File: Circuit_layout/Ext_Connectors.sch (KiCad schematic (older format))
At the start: 9 parts, among them CON1 AVR-JTAG-10, J1 Spare_Conns, J4 Motor_Ctrl, J5 RJ12, P1 TSV, P2 CONN_02X10, P3 CONN_02X07

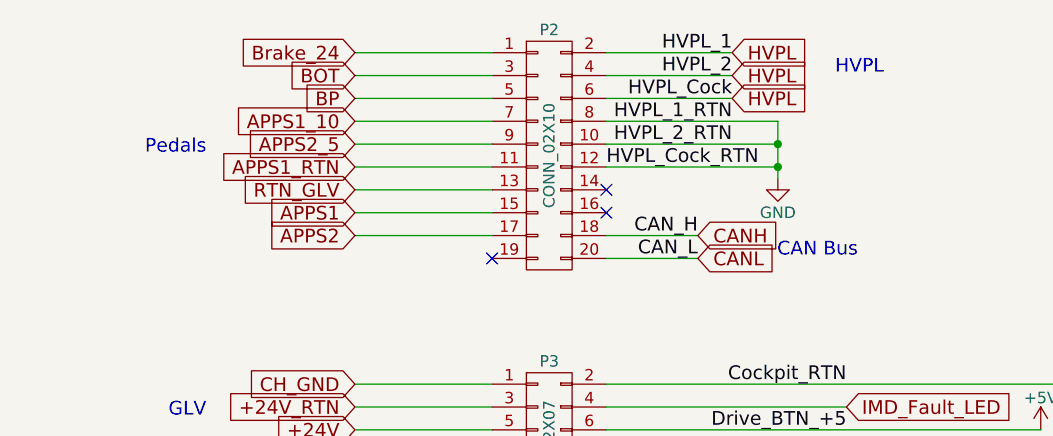
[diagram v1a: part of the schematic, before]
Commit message: organized sheet more, updated some footprints
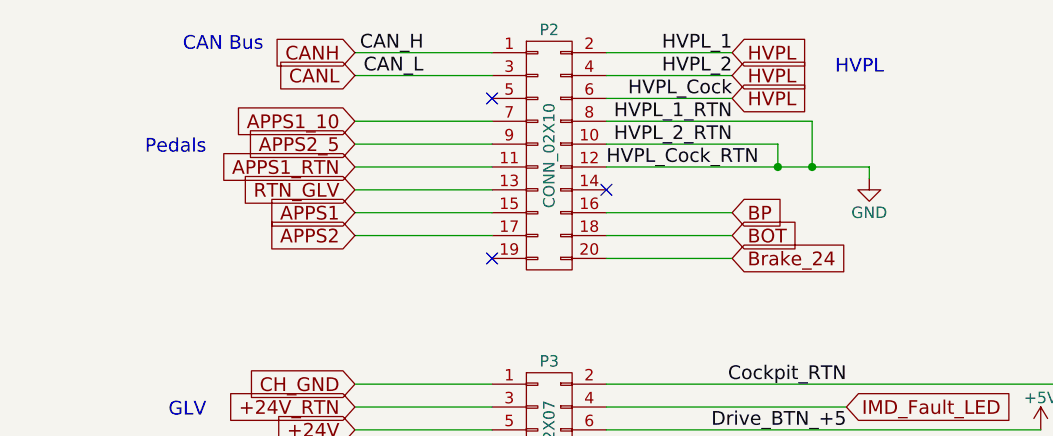
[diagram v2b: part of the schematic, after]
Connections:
- net BOT: now also P2.18 (P18); no longer P2.3 (P3)
- net BP: now also P2.16 (P16); no longer P2.5 (P5)
- net Brake_24: now also P2.20 (P20); no longer P2.1 (P1)
- net CANH: now also P2.1 (P1); no longer P2.18 (P18)
- net CANL: now also P2.3 (P3); no longer P2.20 (P20)
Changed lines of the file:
@@
 Text Label 7750 2700 2    60   ~ 0
 Drive_BTN_+5
-Text Label 7100 1950 2    60   ~ 0
+Text Label 5900 1150 2    60   ~ 0
 CAN_L
-Text Label 7100 1850 2    60   ~ 0
+Text Label 5900 1050 2    60   ~ 0
 CAN_H
 Text Label 7100 3100 2    60   ~ 0
@@
 Text Notes 4800 2900 0    60   ~ 0
 AIRs
-Text Notes 7800 1950 2    60   ~ 0
+Text Notes 5200 1050 2    60   ~ 0
 CAN Bus
 Text GLabel 1900 6450 2    60   Input ~ 0
@@
 Text GLabel 1900 6150 2    60   Input ~ 0
 +5HV
-Text GLabel 5600 1050 0    60   Input ~ 0
+Text GLabel 7250 1950 2    60   Input ~ 0
 Brake_24
-Text GLabel 5600 1150 0    60   Input ~ 0
+Text GLabel 7250 1850 2    60   Input ~ 0
 BOT
 Text GLabel 5600 1350 0    60   Input ~ 0
@@
 ~RESET_AVR
 $Comp
-L +5V #PWR022
+L +5V #PWR020
 U 1 1 58A81530
 P 6800 4400
-F 0 "#PWR022" H 6800 4250 50  0001 C CNN
+F 0 "#PWR020" H 6800 4250 50  0001 C CNN
 F 1 "+5V" H 6800 4540 50  0000 C CNN
 F 2 "" H 6800 4400 50  0000 C CNN
@@
 +24V_RTN
 $Comp
-L +24V #PWR023
+L +24V #PWR021
 U 1 1 58AF1C5B
 P 2250 1250
-F 0 "#PWR023" H 2250 1100 50  0001 C CNN
+F 0 "#PWR021" H 2250 1100 50  0001 C CNN
 F 1 "+24V" H 2250 1390 50  0000 C CNN
 F 2 "" H 2250 1250 50  0000 C CNN
@@
 Drive_LED
 $Comp
-L +5V #PWR024
+L +5V #PWR022
 U 1 1 58B1052B
 P 8600 2700
-F 0 "#PWR024" H 8600 2550 50  0001 C CNN
+F 0 "#PWR022" H 8600 2550 50  0001 C CNN
 F 1 "+5V" H 8600 2840 50  0000 C CNN
 F 2 "" H 8600 2700 50  0000 C CNN
@@
 Throttle_RTN
 $Comp
-L GND #PWR025
+L GND #PWR023
 U 1 1 58B4A72F
 P 7500 3150
-F 0 "#PWR025" H 7500 2900 50  0001 C CNN
+F 0 "#PWR023" H 7500 2900 50  0001 C CNN
 F 1 "GND" H 7500 3000 50  0000 C CNN
 F 2 "" H 7500 3150 50  0000 C CNN
@@
 CH_GND
 $Comp
-L GND #PWR026
+L GND #PWR024
 U 1 1 58B7A0E8
 P 8850 2700
-F 0 "#PWR026" H 8850 2450 50  0001 C CNN
+F 0 "#PWR024" H 8850 2450 50  0001 C CNN
 F 1 "GND" H 8850 2550 50  0000 C CNN
 F 2 "" H 8850 2700 50  0000 C CNN
@@
 CH_GND
 $Comp
-L GND #PWR027
+L GND #PWR025
 U 1 1 58B888D9
 P 2300 1900
-F 0 "#PWR027" H 2300 1650 50  0001 C CNN
+F 0 "#PWR025" H 2300 1650 50  0001 C CNN
 F 1 "GND" H 2300 1750 50  0000 C CNN
 F 2 "" H 2300 1900 50  0000 C CNN
@@
 +24V
 $Comp
-L PWR_FLAG #FLG028
+L PWR_FLAG #FLG026
 U 1 1 58B89230
 P 2550 1250
-F 0 "#FLG028" H 2550 1345 50  0001 C CNN
+F 0 "#FLG026" H 2550 1345 50  0001 C CNN
 F 1 "PWR_FLAG" H 2550 1430 50  0000 C CNN
 F 2 "" H 2550 1250 50  0000 C CNN
@@
 Text GLabel 7250 1250 2    60   Input ~ 0
 HVPL
-Text GLabel 7100 1850 2    60   Input ~ 0
+Text GLabel 5600 1050 0    60   Input ~ 0
 CANH
-Text GLabel 7100 1950 2    60   Input ~ 0
+Text GLabel 5600 1150 0    60   Input ~ 0
 CANL
 Text Notes 4950 2650 2    60   ~ 0
@@
 Spare_ADC_2
 $Comp
-L GND #PWR029
+L GND #PWR027
 U 1 1 58C3E939
-P 7450 1600
-F 0 "#PWR029" H 7450 1350 50  0001 C CNN
-F 1 "GND" H 7450 1450 50  0000 C CNN
-F 2 "" H 7450 1600 50  0000 C CNN
-F 3 "" H 7450 1600 50  0000 C CNN
-	1    7450 1600
+P 7850 1600
+F 0 "#PWR027" H 7850 1350 50  0001 C CNN
+F 1 "GND" H 7850 1450 50  0000 C CNN
+F 2 "" H 7850 1600 50  0000 C CNN
+F 3 "" H 7850 1600 50  0000 C CNN
+	1    7850 1600
 	-1   0    0    -1
 $EndComp
-Text GLabel 5600 1250 0    60   Input ~ 0
+Text GLabel 7250 1750 2    60   Input ~ 0
 BP
 Text Notes 7650 3100 0    60   ~ 0
 RTDS
 $Comp
-L GND #PWR030
+L GND #PWR028
 U 1 1 58D1CF0B
 P 6650 4900
-F 0 "#PWR030" H 6650 4650 50  0001 C CNN
+F 0 "#PWR028" H 6650 4650 50  0001 C CNN
 F 1 "GND" H 6650 4750 50  0000 C CNN
 F 2 "" H 6650 4900 50  0000 C CNN
@@
 I_RTN
 $Comp
-L PWR_FLAG #FLG031
+L PWR_FLAG #FLG029
 U 1 1 58D3F022
 P 2650 1900
-F 0 "#FLG031" H 2650 1995 50  0001 C CNN
+F 0 "#FLG029" H 2650 1995 50  0001 C CNN
 F 1 "PWR_FLAG" H 2650 2080 50  0000 C CNN
 F 2 "" H 2650 1900 50  0000 C CNN
@@
 $EndComp
 $Comp
-L +5V #PWR032
+L +5V #PWR030
 U 1 1 58D6E615
 P 3100 3950
-F 0 "#PWR032" H 3100 3800 50  0001 C CNN
+F 0 "#PWR030" H 3100 3800 50  0001 C CNN
 F 1 "+5V" H 3100 4090 50  0000 C CNN
 F 2 "" H 3100 3950 50  0000 C CNN
@@
 NoConn ~ 6200 1950
 NoConn ~ 6700 1650
-NoConn ~ 6700 1750
 Wire Wire Line
 	1150 6250 1900 6250
@@
 Wire Wire Line
 	6200 1350 5600 1350
-Wire Wire Line
-	6200 1050 5600 1050
 Wire Wire Line
 	1200 7150 1600 7150
@@
 	2250 7000 2250 7250
 Wire Wire Line
-	5600 1150 6200 1150
-Wire Wire Line
 	5600 3100 6200 3100
 Wire Wire Line
@@
 	8850 2500 6700 2500
 Wire Wire Line
-	6700 1950 7100 1950
-Wire Wire Line
-	7100 1850 6700 1850
-Wire Wire Line
 	5600 2600 6200 2600
 Wire Wire Line
@@
 	6700 1150 7250 1150
 Wire Wire Line
-	7450 1350 6700 1350
+	6700 1350 7600 1350
 Wire Wire Line
 	7450 1450 6700 1450
 Wire Wire Line
-	7450 1350 7450 1600
-Connection ~ 7450 1450
-Wire Wire Line
 	7500 3100 6700 3100
 Wire Wire Line
 	6700 3000 7100 3000
-Wire Wire Line
-	5600 1250 6200 1250
 Wire Wire Line
 	7500 3100 7500 3150
@@
 	3100 4050 3100 3950
 Wire Wire Line
-	6700 1550 7450 1550
+	6700 1550 7850 1550
+Wire Wire Line
+	7850 1550 7850 1600
+Wire Wire Line
+	7450 1450 7450 1550
 Connection ~ 7450 1550
+Wire Wire Line
+	7600 1350 7600 1550
+Connection ~ 7600 1550
+Wire Wire Line
+	6700 1750 7250 1750
+Wire Wire Line
+	6700 1850 7250 1850
+Wire Wire Line
+	6700 1950 7250 1950
+Wire Wire Line
+	5600 1150 6200 1150
+Wire Wire Line
+	5600 1050 6200 1050
+NoConn ~ 6200 1250
 $EndSCHEMATC

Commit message: added more tracks
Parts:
- renumbered W16 to +24V1, W17 to CH_GND1
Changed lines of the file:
@@
 ~RESET_AVR
 $Comp
-L +5V #PWR020
+L +5V #PWR022
 U 1 1 58A81530
 P 6800 4400
-F 0 "#PWR020" H 6800 4250 50  0001 C CNN
+F 0 "#PWR022" H 6800 4250 50  0001 C CNN
 F 1 "+5V" H 6800 4540 50  0000 C CNN
 F 2 "" H 6800 4400 50  0000 C CNN
@@
 +24V_RTN
 $Comp
-L +24V #PWR021
+L +24V #PWR023
 U 1 1 58AF1C5B
 P 2250 1250
-F 0 "#PWR021" H 2250 1100 50  0001 C CNN
+F 0 "#PWR023" H 2250 1100 50  0001 C CNN
 F 1 "+24V" H 2250 1390 50  0000 C CNN
 F 2 "" H 2250 1250 50  0000 C CNN
@@
 Drive_LED
 $Comp
-L +5V #PWR022
+L +5V #PWR024
 U 1 1 58B1052B
 P 8600 2700
-F 0 "#PWR022" H 8600 2550 50  0001 C CNN
+F 0 "#PWR024" H 8600 2550 50  0001 C CNN
 F 1 "+5V" H 8600 2840 50  0000 C CNN
 F 2 "" H 8600 2700 50  0000 C CNN
@@
 Throttle_RTN
 $Comp
-L GND #PWR023
+L GND #PWR025
 U 1 1 58B4A72F
 P 7500 3150
-F 0 "#PWR023" H 7500 2900 50  0001 C CNN
+F 0 "#PWR025" H 7500 2900 50  0001 C CNN
 F 1 "GND" H 7500 3000 50  0000 C CNN
 F 2 "" H 7500 3150 50  0000 C CNN
@@
 CH_GND
 $Comp
-L GND #PWR024
+L GND #PWR026
 U 1 1 58B7A0E8
 P 8850 2700
-F 0 "#PWR024" H 8850 2450 50  0001 C CNN
+F 0 "#PWR026" H 8850 2450 50  0001 C CNN
 F 1 "GND" H 8850 2550 50  0000 C CNN
 F 2 "" H 8850 2700 50  0000 C CNN
@@
 CH_GND
 $Comp
-L GND #PWR025
+L GND #PWR027
 U 1 1 58B888D9
 P 2300 1900
-F 0 "#PWR025" H 2300 1650 50  0001 C CNN
+F 0 "#PWR027" H 2300 1650 50  0001 C CNN
 F 1 "GND" H 2300 1750 50  0000 C CNN
 F 2 "" H 2300 1900 50  0000 C CNN
@@
 +24V
 $Comp
-L PWR_FLAG #FLG026
+L PWR_FLAG #FLG028
 U 1 1 58B89230
 P 2550 1250
-F 0 "#FLG026" H 2550 1345 50  0001 C CNN
+F 0 "#FLG028" H 2550 1345 50  0001 C CNN
 F 1 "PWR_FLAG" H 2550 1430 50  0000 C CNN
 F 2 "" H 2550 1250 50  0000 C CNN
@@
 Spare_ADC_2
 $Comp
-L GND #PWR027
+L GND #PWR029
 U 1 1 58C3E939
 P 7850 1600
-F 0 "#PWR027" H 7850 1350 50  0001 C CNN
+F 0 "#PWR029" H 7850 1350 50  0001 C CNN
 F 1 "GND" H 7850 1450 50  0000 C CNN
 F 2 "" H 7850 1600 50  0000 C CNN
@@
 RTDS
 $Comp
-L GND #PWR028
+L GND #PWR030
 U 1 1 58D1CF0B
 P 6650 4900
-F 0 "#PWR028" H 6650 4650 50  0001 C CNN
+F 0 "#PWR030" H 6650 4650 50  0001 C CNN
 F 1 "GND" H 6650 4750 50  0000 C CNN
 F 2 "" H 6650 4900 50  0000 C CNN
@@
 I_RTN
 $Comp
-L PWR_FLAG #FLG029
+L PWR_FLAG #FLG031
 U 1 1 58D3F022
 P 2650 1900
-F 0 "#FLG029" H 2650 1995 50  0001 C CNN
+F 0 "#FLG031" H 2650 1995 50  0001 C CNN
 F 1 "PWR_FLAG" H 2650 2080 50  0000 C CNN
 F 2 "" H 2650 1900 50  0000 C CNN
@@
 $EndComp
 $Comp
-L TEST_1P W16
+L TEST_1P +24V1
 U 1 1 58D4655B
 P 2950 1250
-F 0 "W16" H 2950 1520 50  0000 C CNN
+F 0 "+24V1" H 2950 1520 50  0000 C CNN
 F 1 "+24V" H 2950 1450 50  0000 C CNN
 F 2 "Measurement_Points:Measurement_Point_Round-SMD-Pad_Big" H 3150 1250 50  0001 C CNN
@@
 $EndComp
 $Comp
-L TEST_1P W17
+L TEST_1P CH_GND1
 U 1 1 58D46659
 P 3000 1850
-F 0 "W17" H 3000 2120 50  0000 C CNN
+F 0 "CH_GND1" H 3000 2120 50  0000 C CNN
 F 1 "CH_GND" H 3000 2050 50  0000 C CNN
 F 2 "Measurement_Points:Measurement_Point_Square-SMD-Pad_Big" H 3200 1850 50  0001 C CNN
@@
 $EndComp
 $Comp
-L +5V #PWR030
+L +5V #PWR032
 U 1 1 58D6E615
 P 3100 3950
-F 0 "#PWR030" H 3100 3800 50  0001 C CNN
+F 0 "#PWR032" H 3100 3800 50  0001 C CNN
 F 1 "+5V" H 3100 4090 50  0000 C CNN
 F 2 "" H 3100 3950 50  0000 C CNN

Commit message: working on pcb
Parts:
- J4: footprint custom_footprints:TerminalBlock_Pheonix_MPT-5.08mm_4pol -> custom_footprints:Molex_4x1_2.54mm; Description (none) -> CONN HEADER 4POS .100 VERT GOLD; DigiKey P/N (none) -> WM4802-ND; Man P/N (none) -> 0705430003; Price (none) -> 0.94; URL (none) -> https://www.digikey.com/product-detail/en/molex-llc/0705430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; Wire Number W-21 -> (none)
- P1: footprint custom_footprints:TerminalBlock_Pheonix_MPT-5.08mm_2pol -> custom_footprints:AMPCONN_2; Description (none) -> CONN RCPT 2POS 11.18MM PCB SLDR; DigiKey P/N (none) -> A113980-ND; Man P/N (none) -> 556881-2; Price (none) -> 7.13; URL (none) -> https://www.digikey.com/product-detail/en/te-connectivity-a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
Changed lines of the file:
@@
 F 0 "J4" H 950 6550 50  0000 C CNN
 F 1 "Motor_Ctrl" V 1050 6300 50  0000 C CNN
-F 2 "custom_footprints:TerminalBlock_Pheonix_MPT-5.08mm_4pol" H 50  6600 50  0001 C CNN
+F 2 "custom_footprints:Molex_4x1_2.54mm" H 50  6600 50  0001 C CNN
 F 3 "" H 950 6300 50  0000 C CNN
-F 4 "W-21" H 950 6300 60  0001 C CNN "Wire Number"
+F 4 "WM4802-ND" H 950 6300 60  0001 C CNN "DigiKey P/N"
+F 5 "https://www.digikey.com/product-detail/en/molex-llc/0705430003/WM4802-ND/114923" H 950 6300 60  0001 C CNN "URL"
+F 6 "0705430003" H 950 6300 60  0001 C CNN "Man P/N"
+F 7 "CONN HEADER 4POS .100 VERT GOLD" H 950 6300 60  0001 C CNN "Description"
+F 8 "0.94" H 950 6300 60  0001 C CNN "Price"
 	1    950  6300
 	-1   0    0    1
@@
 F 0 "P1" H 1000 7250 50  0000 C CNN
 F 1 "TSV" V 1100 7100 50  0000 C CNN
-F 2 "custom_footprints:TerminalBlock_Pheonix_MPT-5.08mm_2pol" H 1000 7100 50  0001 C CNN
+F 2 "custom_footprints:AMPCONN_2" H 1000 7100 50  0001 C CNN
 F 3 "" H 1000 7100 50  0000 C CNN
+F 4 "A113980-ND" H 1000 7100 60  0001 C CNN "DigiKey P/N"
+F 5 "https://www.digikey.com/product-detail/en/te-connectivity-amp-connectors/556881-2/A113980-ND/294120" H 1000 7100 60  0001 C CNN "URL"
+F 6 "556881-2" H 1000 7100 60  0001 C CNN "Man P/N"
+F 7 "CONN RCPT 2POS 11.18MM PCB SLDR" H 1000 7100 60  0001 C CNN "Description"
+F 8 "7.13" H 1000 7100 60  0001 C CNN "Price"
 	1    1000 7100
 	-1   0    0    1

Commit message: review pcb, made notes
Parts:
- removed CH_GND1: CH_GND, Measurement_Points:Measurement_Point_Square-SMD-Pad_Big, symbol TEST_1P
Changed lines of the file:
@@
-$EndComp
-$Comp
-L TEST_1P CH_GND1
-U 1 1 58D46659
-P 3000 1850
-F 0 "CH_GND1" H 3000 2120 50  0000 C CNN
-F 1 "CH_GND" H 3000 2050 50  0000 C CNN
-F 2 "Measurement_Points:Measurement_Point_Square-SMD-Pad_Big" H 3200 1850 50  0001 C CNN
-F 3 "" H 3200 1850 50  0000 C CNN
-	1    3000 1850
-	-1   0    0    1
 $EndComp
 $Comp
@@
 	2800 3700 2800 4050
 Wire Wire Line
-	2100 1650 3000 1650
-Wire Wire Line
 	2300 1650 2300 1900
 Wire Wire Line
@@
 Wire Wire Line
 	2650 1650 2650 1900
-Wire Wire Line
-	3000 1650 3000 1850
 Connection ~ 2650 1650
 Wire Wire Line
@@
 	5600 1050 6200 1050
 NoConn ~ 6200 1250
+Wire Wire Line
+	2100 1650 2650 1650
 $EndSCHEMATC

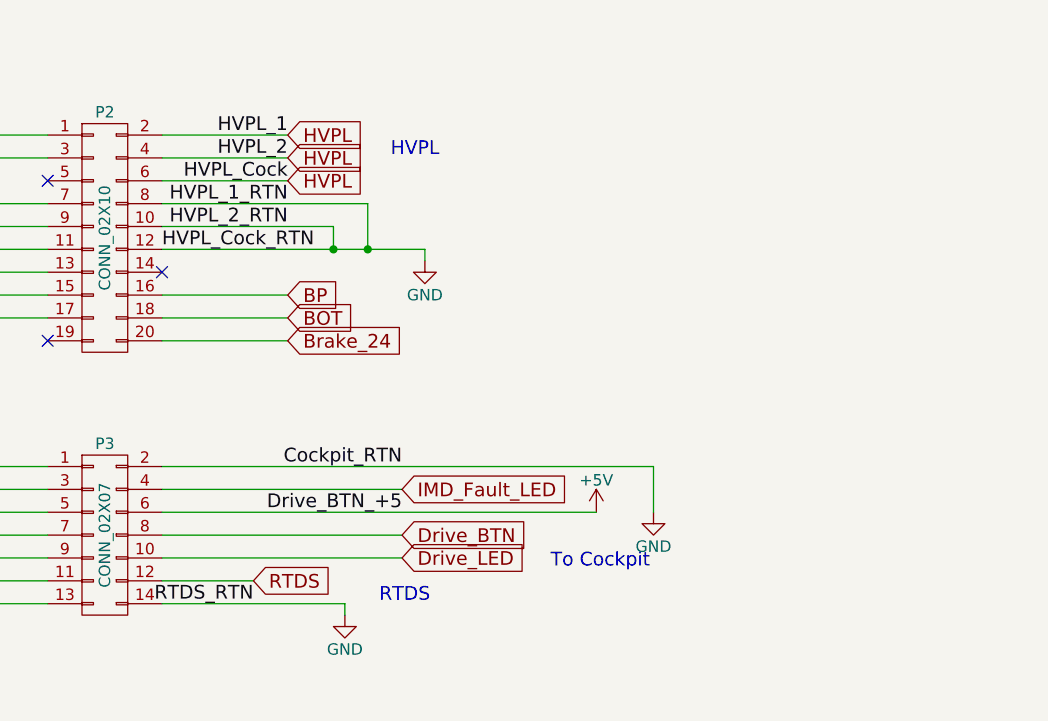
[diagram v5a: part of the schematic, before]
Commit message: fixed changes proposed by prof. nadovich.
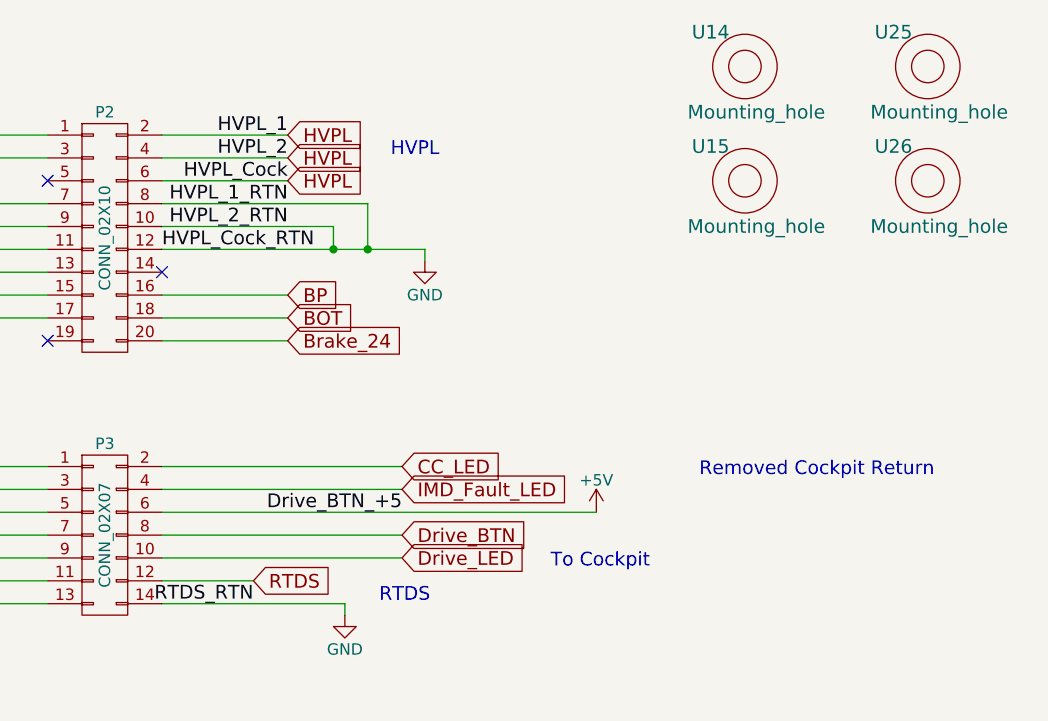
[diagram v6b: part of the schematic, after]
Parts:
- added U14, U15, U25, U26: Mounting_hole, Mounting_Holes:MountingHole_3.5mm_Pad, symbol Mounting_hole
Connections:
- net GND: no longer P3.2 (P2)
- new net CC_LED: P3.2 (P2)
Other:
- note added: "Removed Cockpit Return"
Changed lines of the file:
@@
 ~RESET_AVR
 $Comp
-L +5V #PWR022
+L +5V #PWR028
 U 1 1 58A81530
 P 6800 4400
-F 0 "#PWR022" H 6800 4250 50  0001 C CNN
+F 0 "#PWR028" H 6800 4250 50  0001 C CNN
 F 1 "+5V" H 6800 4540 50  0000 C CNN
 F 2 "" H 6800 4400 50  0000 C CNN
@@
 +24V_RTN
 $Comp
-L +24V #PWR023
+L +24V #PWR029
 U 1 1 58AF1C5B
 P 2250 1250
-F 0 "#PWR023" H 2250 1100 50  0001 C CNN
+F 0 "#PWR029" H 2250 1100 50  0001 C CNN
 F 1 "+24V" H 2250 1390 50  0000 C CNN
 F 2 "" H 2250 1250 50  0000 C CNN
@@
 Drive_LED
 $Comp
-L +5V #PWR024
+L +5V #PWR030
 U 1 1 58B1052B
 P 8600 2700
-F 0 "#PWR024" H 8600 2550 50  0001 C CNN
+F 0 "#PWR030" H 8600 2550 50  0001 C CNN
 F 1 "+5V" H 8600 2840 50  0000 C CNN
 F 2 "" H 8600 2700 50  0000 C CNN
@@
 Throttle_RTN
 $Comp
-L GND #PWR025
+L GND #PWR031
 U 1 1 58B4A72F
 P 7500 3150
-F 0 "#PWR025" H 7500 2900 50  0001 C CNN
+F 0 "#PWR031" H 7500 2900 50  0001 C CNN
 F 1 "GND" H 7500 3000 50  0000 C CNN
 F 2 "" H 7500 3150 50  0000 C CNN
@@
 Text GLabel 5600 2500 0    60   Input ~ 0
 CH_GND
-$Comp
-L GND #PWR026
-U 1 1 58B7A0E8
-P 8850 2700
-F 0 "#PWR026" H 8850 2450 50  0001 C CNN
-F 1 "GND" H 8850 2550 50  0000 C CNN
-F 2 "" H 8850 2700 50  0000 C CNN
-F 3 "" H 8850 2700 50  0000 C CNN
-	1    8850 2700
-	-1   0    0    -1
-$EndComp
 Text GLabel 2100 1650 0    60   Input ~ 0
 CH_GND
 $Comp
-L GND #PWR027
+L GND #PWR032
 U 1 1 58B888D9
 P 2300 1900
-F 0 "#PWR027" H 2300 1650 50  0001 C CNN
+F 0 "#PWR032" H 2300 1650 50  0001 C CNN
 F 1 "GND" H 2300 1750 50  0000 C CNN
 F 2 "" H 2300 1900 50  0000 C CNN
@@
 +24V
 $Comp
-L PWR_FLAG #FLG028
+L PWR_FLAG #FLG033
 U 1 1 58B89230
 P 2550 1250
-F 0 "#FLG028" H 2550 1345 50  0001 C CNN
+F 0 "#FLG033" H 2550 1345 50  0001 C CNN
 F 1 "PWR_FLAG" H 2550 1430 50  0000 C CNN
 F 2 "" H 2550 1250 50  0000 C CNN
@@
 Text Notes 4950 2650 2    60   ~ 0
 GLV
-Text Label 7750 2500 2    60   ~ 0
-Cockpit_RTN
 Text GLabel 5600 1450 0    60   Input ~ 0
 APPS2_5
@@
 Spare_ADC_2
 $Comp
-L GND #PWR029
+L GND #PWR034
 U 1 1 58C3E939
 P 7850 1600
-F 0 "#PWR029" H 7850 1350 50  0001 C CNN
+F 0 "#PWR034" H 7850 1350 50  0001 C CNN
 F 1 "GND" H 7850 1450 50  0000 C CNN
 F 2 "" H 7850 1600 50  0000 C CNN
@@
 RTDS
 $Comp
-L GND #PWR030
+L GND #PWR035
 U 1 1 58D1CF0B
 P 6650 4900
-F 0 "#PWR030" H 6650 4650 50  0001 C CNN
+F 0 "#PWR035" H 6650 4650 50  0001 C CNN
 F 1 "GND" H 6650 4750 50  0000 C CNN
 F 2 "" H 6650 4900 50  0000 C CNN
@@
 I_RTN
 $Comp
-L PWR_FLAG #FLG031
+L PWR_FLAG #FLG036
 U 1 1 58D3F022
 P 2650 1900
-F 0 "#FLG031" H 2650 1995 50  0001 C CNN
+F 0 "#FLG036" H 2650 1995 50  0001 C CNN
 F 1 "PWR_FLAG" H 2650 2080 50  0000 C CNN
 F 2 "" H 2650 1900 50  0000 C CNN
@@
 $EndComp
 $Comp
-L +5V #PWR032
+L +5V #PWR037
 U 1 1 58D6E615
 P 3100 3950
-F 0 "#PWR032" H 3100 3800 50  0001 C CNN
+F 0 "#PWR037" H 3100 3800 50  0001 C CNN
 F 1 "+5V" H 3100 4090 50  0000 C CNN
 F 2 "" H 3100 3950 50  0000 C CNN
@@
 	5600 2700 6200 2700
 Wire Wire Line
-	8850 2500 6700 2500
-Wire Wire Line
 	5600 2600 6200 2600
 Wire Wire Line
@@
 Wire Wire Line
 	7500 3100 7500 3150
-Wire Wire Line
-	8850 2500 8850 2700
 Connection ~ 2300 1650
 Wire Wire Line
@@
 Wire Wire Line
 	2100 1650 2650 1650
+$Comp
+L Mounting_hole U14
+U 1 1 58DA09CC
+P 9250 750
+F 0 "U14" H 9100 900 60  0000 C CNN
+F 1 "Mounting_hole" H 9300 550 60  0000 C CNN
+F 2 "Mounting_Holes:MountingHole_3.5mm_Pad" H 9250 750 60  0001 C CNN
+F 3 "" H 9250 750 60  0000 C CNN
+	1    9250 750
+	1    0    0    -1
+$EndComp
+$Comp
+L Mounting_hole U15
+U 1 1 58DA0CCF
+P 9250 1250
+F 0 "U15" H 9100 1400 60  0000 C CNN
+F 1 "Mounting_hole" H 9300 1050 60  0000 C CNN
+F 2 "Mounting_Holes:MountingHole_3.5mm_Pad" H 9250 1250 60  0001 C CNN
+F 3 "" H 9250 1250 60  0000 C CNN
+	1    9250 1250
+	1    0    0    -1
+$EndComp
+$Comp
+L Mounting_hole U26
+U 1 1 58DA0D11
+P 10050 1250
+F 0 "U26" H 9900 1400 60  0000 C CNN
+F 1 "Mounting_hole" H 10100 1050 60  0000 C CNN
+F 2 "Mounting_Holes:MountingHole_3.5mm_Pad" H 10050 1250 60  0001 C CNN
+F 3 "" H 10050 1250 60  0000 C CNN
+	1    10050 1250
+	1    0    0    -1
+$EndComp
+$Comp
+L Mounting_hole U25
+U 1 1 58DA0D7E
+P 10050 750
+F 0 "U25" H 9900 900 60  0000 C CNN
+F 1 "Mounting_hole" H 10100 550 60  0000 C CNN
+F 2 "Mounting_Holes:MountingHole_3.5mm_Pad" H 10050 750 60  0001 C CNN
+F 3 "" H 10050 750 60  0000 C CNN
+	1    10050 750
+	1    0    0    -1
+$EndComp
+Text Notes 9050 2550 0    60   ~ 0
+Removed Cockpit Return
+Text GLabel 7750 2500 2    60   Input ~ 0
+CC_LED
+Wire Wire Line
+	7750 2500 6700 2500
 $EndSCHEMATC
